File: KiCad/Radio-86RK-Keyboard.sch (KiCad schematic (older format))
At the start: 95 parts, among them J4 Cassette, SW1 FF, SW10 ВК CR, SW11 ЗБ DEL, SW12 LEFT, SW13 UP, SW14 RIGHT, SW15 DOWN, SW16 0, SW17 1 !, SW18 2 \", SW19 3 #, SW2 СТР CLS, SW20 4 $, SW21 5 %, SW22 6 &, SW23 7 ', SW24 8 (, SW25 9 ), SW26 : *, SW27 ; +, SW28 , <, SW29 - =, SW3 АР2 ESC, SW30 . >, SW31 / ?, SW32 Ю @, SW33 А A, SW34 Б B, SW35 Ц C, SW36 Д D, SW37 Е E, SW38 Ф F, SW39 Г G, SW4 F1, SW40 Х H, SW41 И I, SW42 Й J, SW43 К K, SW44 Л L, SW45 М M, SW46 Н N, SW47 О O, SW48 П P, SW49 Я Q, SW5 F2, SW50 Р R, SW51 С S, SW52 Т T, SW53 У U, SW54 Ж V, SW55 В W, SW56 X Ь, SW57 Ы Y, SW58 З Z, SW59 Ш [, SW6 F3, SW60 Э \\, SW61 Щ ], SW62 Ч ^, SW63 SPACE, SW64 УС CTRL, SW65 CC GRAPH, SW66 RUS/LAT, SW7 F4, SW8 ТАБ TAB, SW9 ПС LF, U19 7404/К155ЛН1, U21 TL071/К140УД6, U5 8255A/КР580ВВ55А

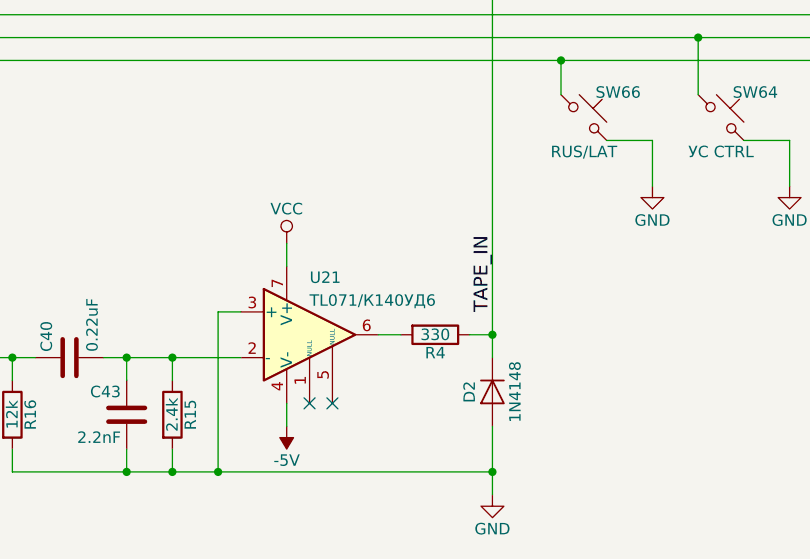
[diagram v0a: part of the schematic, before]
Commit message: Change 8224 package to DIP16; Swap Down/Right keys; Fix U21 soviet designation
Signed-off-by: Sergey Kiselev <skiselev@gmail.com>
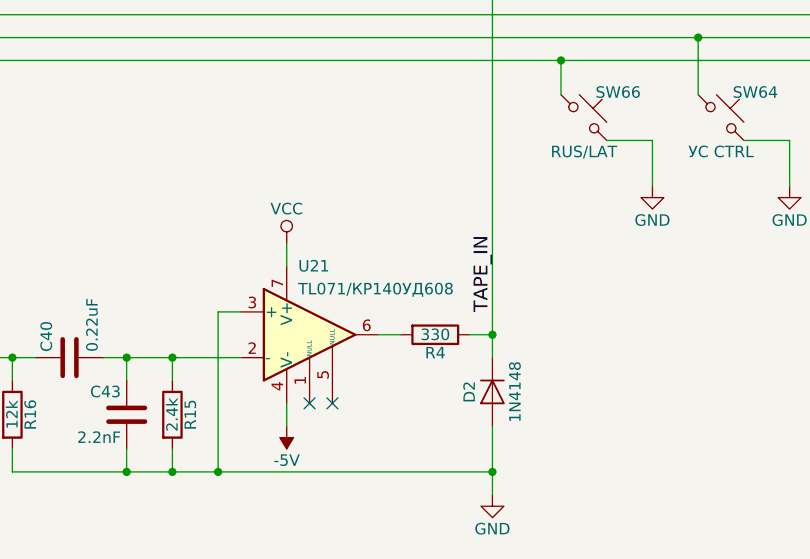
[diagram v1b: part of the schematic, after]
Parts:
- U21: value TL071/К140УД6 -> TL071/КР140УД608
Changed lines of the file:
@@
 AR Path="/5F07BF1C" Ref="U?"  Part="1"
 AR Path="/5E1E4EF5/5F07BF1C" Ref="U21"  Part="1"
-F 0 "U21" H 5100 7350 50  0000 L CNN
-F 1 "TL071/К140УД6" H 5100 7250 50  0000 L CNN
+F 0 "U21" H 5050 7400 50  0000 L CNN
+F 1 "TL071/КР140УД608" H 5050 7300 50  0000 L CNN
 F 2 "My_Components:IC_DIP8_300" H 5150 7300 50  0001 C CNN
 F 3 "" H 5100 7350 50  0000 C CNN

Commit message: Update design files to v1.1
Signed-off-by: Sergey Kiselev <skiselev@gmail.com>
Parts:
- renumbered C40 to C39, C43 to C42, D2 to D1, D11 to D10, D12 to D11, D3 to D2, D4 to D3, D5 to D4, D6 to D5, D7 to D6, D8 to D7, D9 to D8, D10 to D9, R15 to R14, R16 to R15
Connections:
- net D12+ is gone; now on net D11+: D11.2 (A), R13.2
- net D11+: no longer D10.2 (A), R12.2
- new net D10+: D10.2 (A), R12.2
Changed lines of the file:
@@
 $EndComp
 $Comp
-L Device:D D4
+L Device:D D3
 U 1 1 5A6E77A6
 P 4550 1200
-F 0 "D4" H 4550 1300 50  0000 C CNN
+F 0 "D3" H 4550 1300 50  0000 C CNN
 F 1 "1N4148" H 4550 1100 50  0000 C CNN
 F 2 "My_Components:Diode_762" H 4550 1200 50  0001 C CNN
@@
 $EndComp
 $Comp
-L Device:D D5
+L Device:D D4
 U 1 1 5A6E7B0A
 P 4550 1700
-F 0 "D5" H 4550 1800 50  0000 C CNN
+F 0 "D4" H 4550 1800 50  0000 C CNN
 F 1 "1N4148" H 4550 1600 50  0000 C CNN
 F 2 "My_Components:Diode_762" H 4550 1700 50  0001 C CNN
@@
 $EndComp
 $Comp
-L Device:D D6
+L Device:D D5
 U 1 1 5A6E7BF3
 P 4550 2200
-F 0 "D6" H 4550 2300 50  0000 C CNN
+F 0 "D5" H 4550 2300 50  0000 C CNN
 F 1 "1N4148" H 4550 2100 50  0000 C CNN
 F 2 "My_Components:Diode_762" H 4550 2200 50  0001 C CNN
@@
 $EndComp
 $Comp
-L Device:LED D12
+L Device:LED D11
 U 1 1 5A7064C8
 P 2450 1600
-F 0 "D12" H 2450 1700 50  0000 C CNN
+F 0 "D11" H 2450 1700 50  0000 C CNN
 F 1 "RUS/LAT" H 2550 1500 50  0000 C CNN
 F 2 "My_Components:LED_3mm" H 2450 1600 50  0001 C CNN
@@
 $EndComp
 $Comp
-L Device:LED D11
+L Device:LED D10
 U 1 1 5A7067B2
 P 2450 2000
-F 0 "D11" H 2450 2100 50  0000 C CNN
+F 0 "D10" H 2450 2100 50  0000 C CNN
 F 1 "POWER" H 2500 1900 50  0000 C CNN
 F 2 "My_Components:LED_3mm" H 2450 2000 50  0001 C CNN
@@
 ROW7
 Text Label 2600 2000 0    60   ~ 0
+D10+
+Text Label 2600 1600 0    60   ~ 0
 D11+
-Text Label 2600 1600 0    60   ~ 0
-D12+
 Wire Wire Line
 	4800 700  5400 700
@@
 	4800 3700 5400 3700
 $Comp
-L Device:D D3
+L Device:D D2
 U 1 1 5E28C1DF
 P 4550 700
-F 0 "D3" H 4550 800 50  0000 C CNN
+F 0 "D2" H 4550 800 50  0000 C CNN
 F 1 "1N4148" H 4550 600 50  0000 C CNN
 F 2 "My_Components:Diode_762" H 4550 700 50  0001 C CNN
@@
 $EndComp
 $Comp
-L Device:D D8
+L Device:D D7
 U 1 1 5E28DCD3
 P 4550 3200
-F 0 "D8" H 4550 3300 50  0000 C CNN
+F 0 "D7" H 4550 3300 50  0000 C CNN
 F 1 "1N4148" H 4550 3100 50  0000 C CNN
 F 2 "My_Components:Diode_762" H 4550 3200 50  0001 C CNN
@@
 $EndComp
 $Comp
-L Device:D D9
+L Device:D D8
 U 1 1 5E28DCDD
 P 4550 3700
-F 0 "D9" H 4550 3800 50  0000 C CNN
+F 0 "D8" H 4550 3800 50  0000 C CNN
 F 1 "1N4148" H 4550 3600 50  0000 C CNN
 F 2 "My_Components:Diode_762" H 4550 3700 50  0001 C CNN
@@
 $EndComp
 $Comp
-L Device:D D10
+L Device:D D9
 U 1 1 5E28DCE7
 P 4550 4200
-F 0 "D10" H 4550 4300 50  0000 C CNN
+F 0 "D9" H 4550 4300 50  0000 C CNN
 F 1 "1N4148" H 4550 4100 50  0000 C CNN
 F 2 "My_Components:Diode_762" H 4550 4200 50  0001 C CNN
@@
 $EndComp
 $Comp
-L Device:D D7
+L Device:D D6
 U 1 1 5E28DCF1
 P 4550 2700
-F 0 "D7" H 4550 2800 50  0000 C CNN
+F 0 "D6" H 4550 2800 50  0000 C CNN
 F 1 "1N4148" H 4550 2600 50  0000 C CNN
 F 2 "My_Components:Diode_762" H 4550 2700 50  0001 C CNN
@@
 P 4050 7200
 AR Path="/5F07BEF7" Ref="C?"  Part="1"
-AR Path="/5E1E4EF5/5F07BEF7" Ref="C40"  Part="1"
-F 0 "C40" H 4075 7300 50  0000 L CNN
+AR Path="/5E1E4EF5/5F07BEF7" Ref="C39"  Part="1"
+F 0 "C39" H 4075 7300 50  0000 L CNN
 F 1 "0.22uF" H 4075 7100 50  0000 L CNN
 F 2 "My_Components:Cap_Cer_508" H 4088 7050 50  0001 C CNN
@@
 P 4300 7450
 AR Path="/5F07BEFD" Ref="C?"  Part="1"
-AR Path="/5E1E4EF5/5F07BEFD" Ref="C43"  Part="1"
-F 0 "C43" H 4325 7550 50  0000 L CNN
+AR Path="/5E1E4EF5/5F07BEFD" Ref="C42"  Part="1"
+F 0 "C42" H 4325 7550 50  0000 L CNN
 F 1 "2.2nF" H 4325 7350 50  0000 L CNN
 F 2 "My_Components:Cap_Cer_508" H 4338 7300 50  0001 C CNN
@@
 P 3800 7450
 AR Path="/5F07BF03" Ref="R?"  Part="1"
-AR Path="/5E1E4EF5/5F07BF03" Ref="R16"  Part="1"
-F 0 "R16" V 3880 7450 50  0000 C CNN
+AR Path="/5E1E4EF5/5F07BF03" Ref="R15"  Part="1"
+F 0 "R15" V 3880 7450 50  0000 C CNN
 F 1 "12k" V 3800 7450 50  0000 C CNN
 F 2 "My_Components:Res_762" V 3730 7450 50  0001 C CNN
@@
 P 4500 7450
 AR Path="/5F07BF09" Ref="R?"  Part="1"
-AR Path="/5E1E4EF5/5F07BF09" Ref="R15"  Part="1"
-F 0 "R15" V 4580 7450 50  0000 C CNN
+AR Path="/5E1E4EF5/5F07BF09" Ref="R14"  Part="1"
+F 0 "R14" V 4580 7450 50  0000 C CNN
 F 1 "2.4k" V 4500 7450 50  0000 C CNN
 F 2 "My_Components:Res_762" V 4430 7450 50  0001 C CNN
@@
 P 5900 7350
 AR Path="/5F07BF16" Ref="D?"  Part="1"
-AR Path="/5E1E4EF5/5F07BF16" Ref="D2"  Part="1"
-F 0 "D2" H 5900 7450 50  0000 C CNN
+AR Path="/5E1E4EF5/5F07BF16" Ref="D1"  Part="1"
+F 0 "D1" H 5900 7450 50  0000 C CNN
 F 1 "1N4148" H 5900 7250 50  0000 C CNN
 F 2 "My_Components:Diode_762" H 5900 7350 50  0001 C CNN
